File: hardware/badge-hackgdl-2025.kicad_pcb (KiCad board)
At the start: 11 copper layers, 73.4 x 79.5 mm, 57 parts, among them J1 ADDON, J2 Battery, P1 USB_C_Plug_USB2.0, Q1 DMG3415U-7, Q2 MMBT2222A, SW1 ON, SW2 RESET, SW3 BOOT, SW4 RIGHT, SW5 BACK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

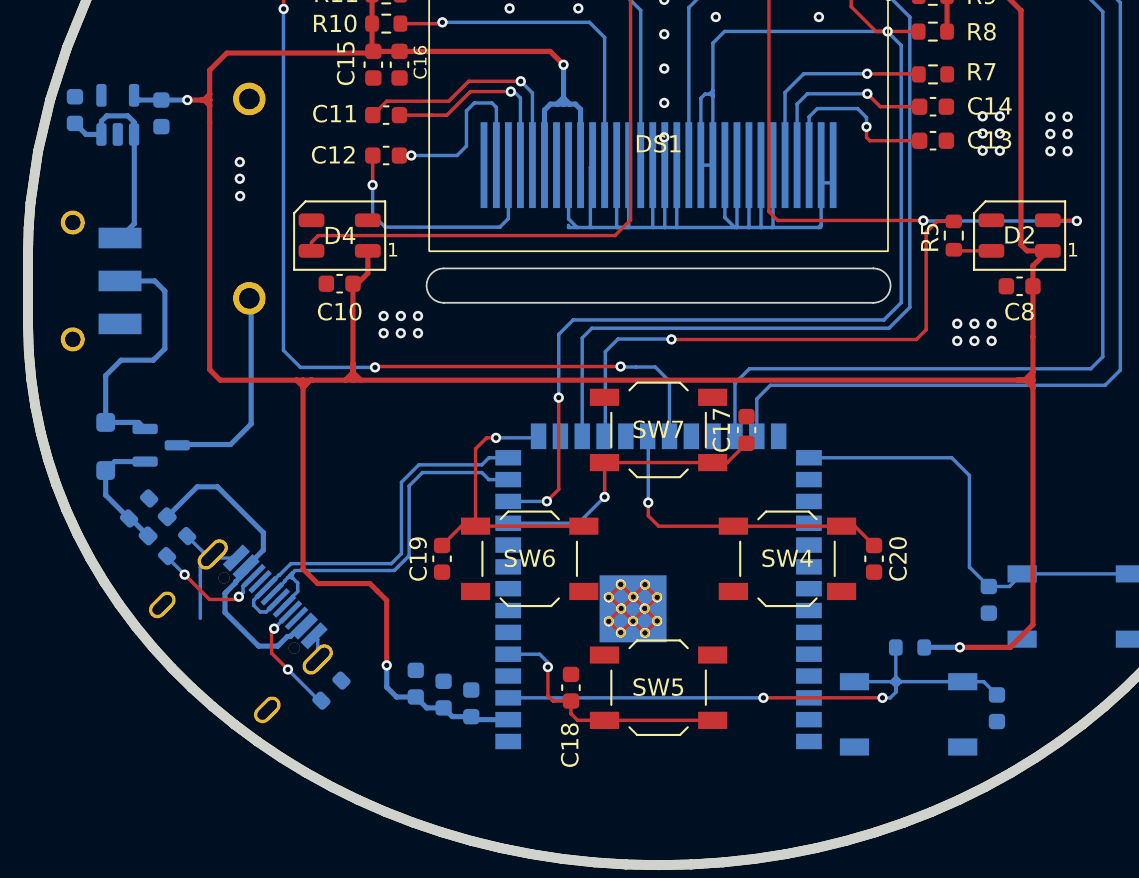
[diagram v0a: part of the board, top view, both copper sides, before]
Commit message: feat(hw): add space between buttons
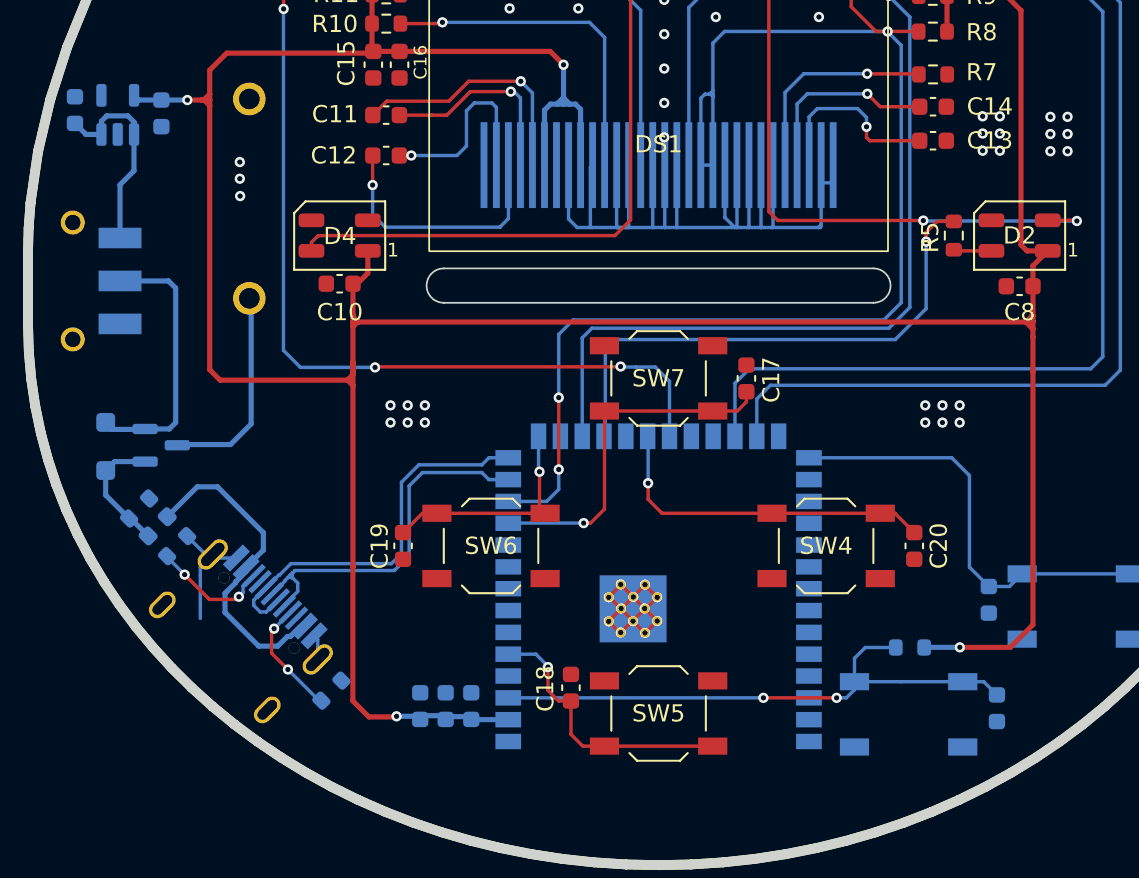
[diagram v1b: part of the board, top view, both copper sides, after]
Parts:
- moved C17 3.00 mm to (138.8, 70.0)
- moved SW7 3.00 mm to (133.7, 70.0)
- moved C20 2.46 mm to (148.6, 79.8)
- moved C19 2.39 mm to (118.8, 79.8)
- moved SW4 2.37 mm to (143.4, 79.8)
- moved SW6 2.37 mm to (123.9, 79.8)
- moved SW5 1.50 mm to (133.7, 89.5)
- moved C3 1.33 mm to (119.8, 89.1)
- moved C4 0.68 mm to (121.3, 89.1)
- moved C5 0.16 mm to (122.8, 89.1)
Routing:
- net /MIDDLE: track 17.0 -> 20.7 mm
- net /LEFT: track 17.2 -> 13.5 mm
- net +3V3: track 250.7 -> 247.8 mm
- net /RST: track 36.2 -> 33.4 mm
- net /RIGHT: track 18.5 -> 20.0 mm
- net /BACK: track 15.1 -> 16.1 mm
- net /NEOPIXEL: track 31.7 -> 31.0 mm
- net GND: track 99.6 -> 98.9 mm

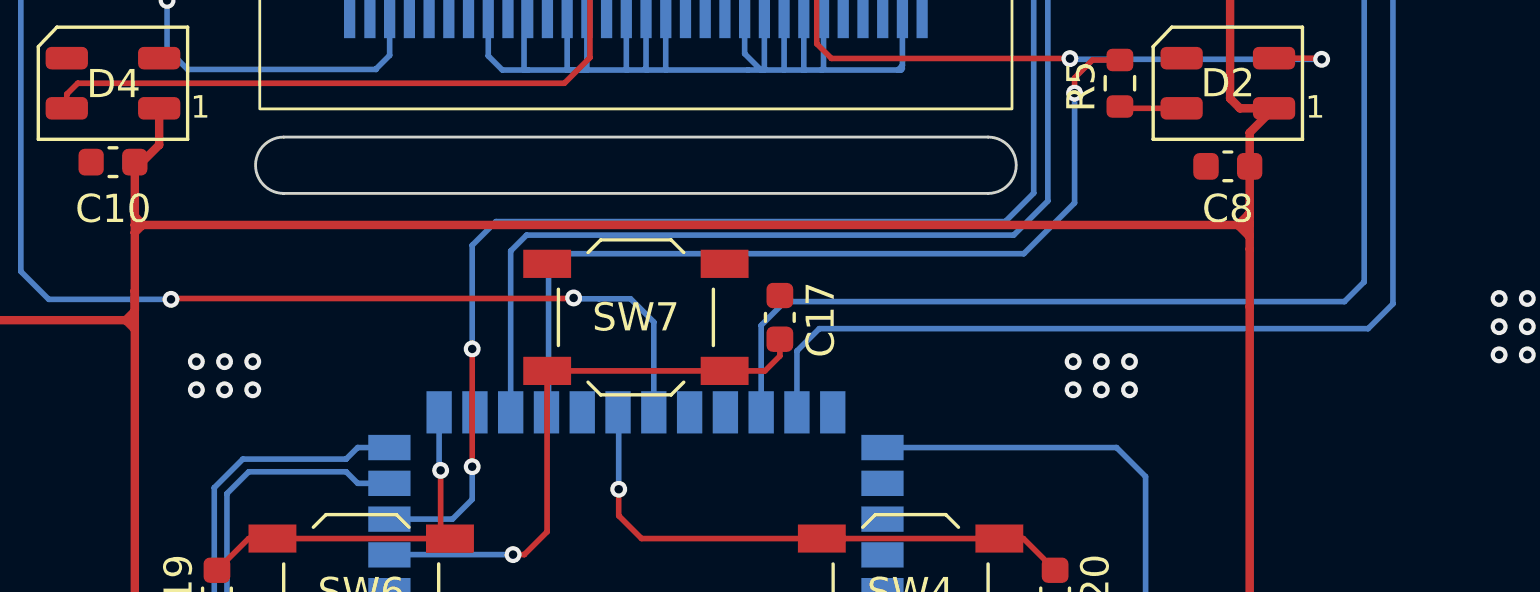
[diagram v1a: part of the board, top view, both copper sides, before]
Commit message: fix(hw): change gpio pins for addon connector
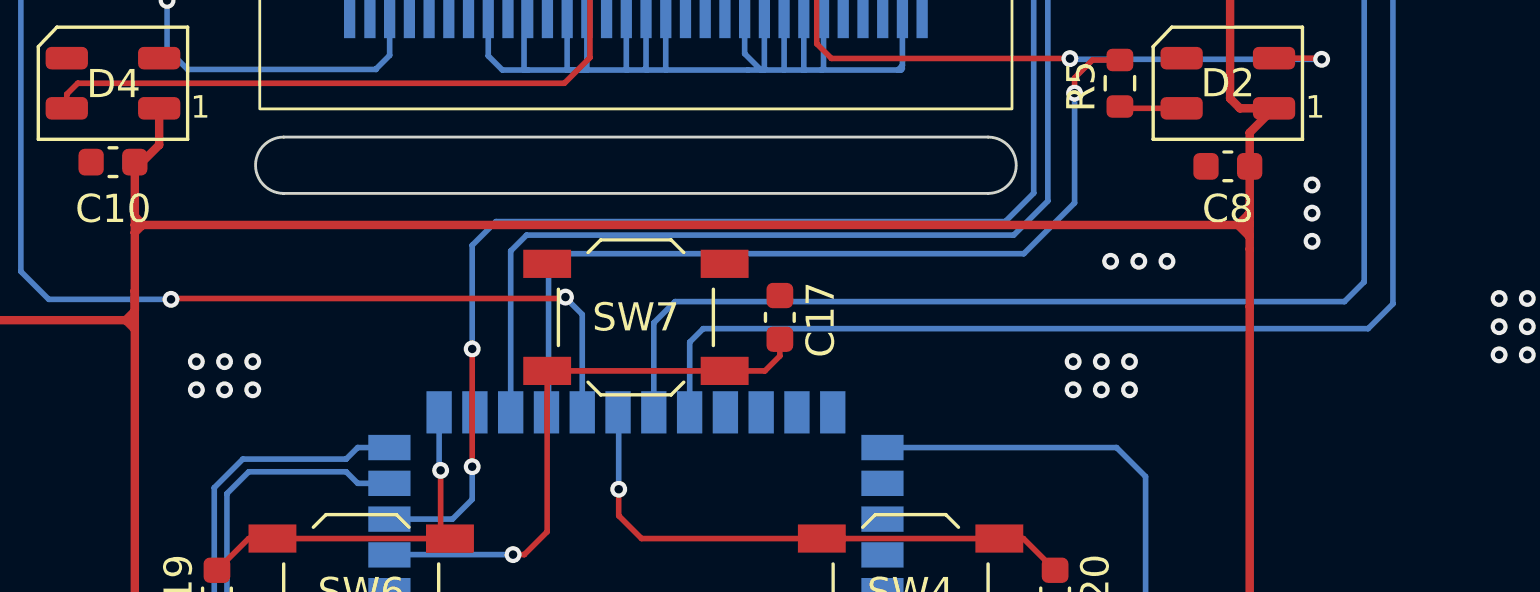
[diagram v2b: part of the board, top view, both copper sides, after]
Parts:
- removed kibuzzard-67869934: G***, kibuzzard-67869934
- removed kibuzzard-67869944: G***, kibuzzard-67869944
- removed kibuzzard-678699AD: G***, kibuzzard-678699AD
- removed kibuzzard-678699B2: G***, kibuzzard-678699B2
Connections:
- U2 pad 19: unconnected-(U2-IO11-Pad19) -> /Buzz
- U2 pad 21: /Buzz -> /GPIO2
- U2 pad 22: unconnected-(U2-IO14-Pad22) -> /GPIO1
- U2 pad 24: /GPIO2 -> unconnected-(U2-IO47-Pad24)
- U2 pad 25: /GPIO1 -> unconnected-(U2-IO48-Pad25)
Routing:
- net /GPIO1: track 73.0 -> 77.0 mm
- net /GPIO2: track 67.6 -> 71.5 mm
- net /Buzz: track 49.6 -> 47.3 mm
- net GND: vias 93 -> 99

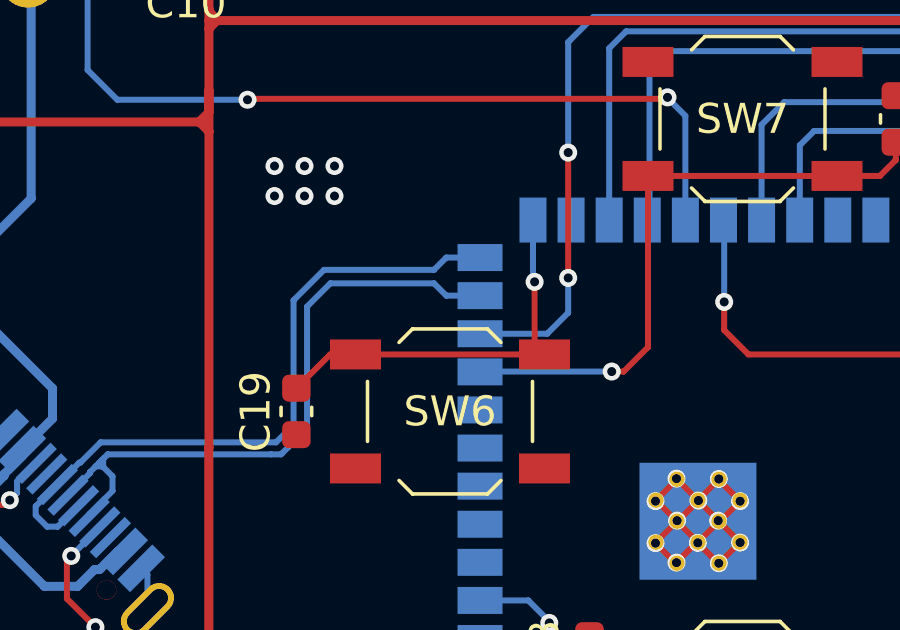
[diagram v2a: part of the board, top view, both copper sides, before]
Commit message: fix(hw): change left button to gpio 17
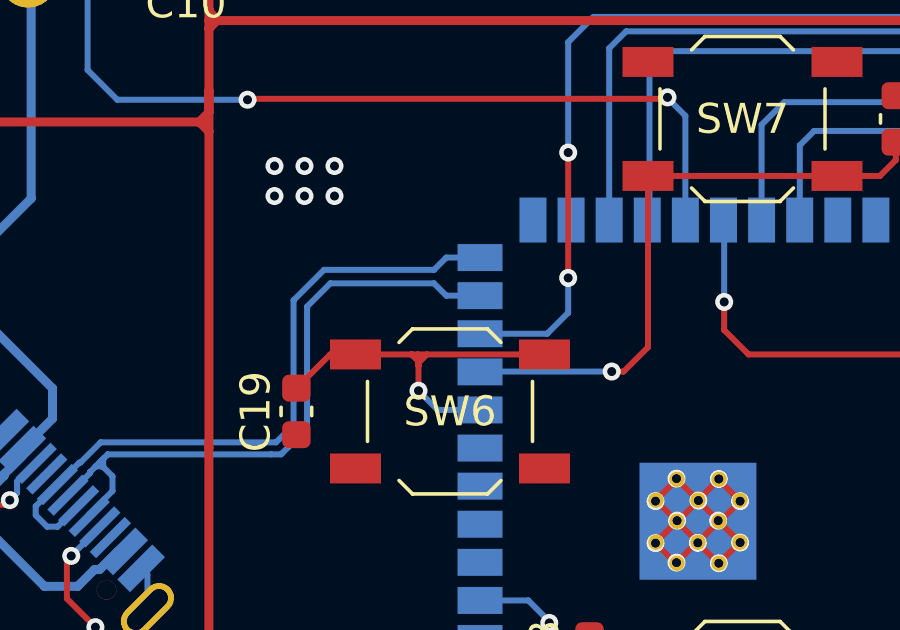
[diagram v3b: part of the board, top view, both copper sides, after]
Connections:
- U2 pad 10: unconnected-(U2-IO17-Pad10) -> /LEFT
- U2 pad 15: /LEFT -> unconnected-(U2-IO3-Pad15)
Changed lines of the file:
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@@
 	(net 59 "unconnected-(U2-IO39-Pad32)")
 	(net 60 "unconnected-(U2-IO36-Pad29)")
-	(net 61 "unconnected-(U2-IO17-Pad10)")
+	(net 61 "unconnected-(U2-IO3-Pad15)")
 	(net 62 "unconnected-(U2-IO15-Pad8)")
 	(net 63 "unconnected-(U2-IO47-Pad24)")
@@
 			(size 1.5 0.9)
 			(layers "B.Cu" "B.Mask" "B.Paste")
-			(net 61 "unconnected-(U2-IO17-Pad10)")
+			(net 16 "/LEFT")
 			(pinfunction "IO17")
-			(pintype "bidirectional+no_connect")
+			(pintype "bidirectional")
 		)
 		(pad "11" smd rect
@@
 			(size 1.5 0.9)
 			(layers "B.Cu" "B.Mask" "B.Paste")
-			(net 16 "/LEFT")
+			(net 61 "unconnected-(U2-IO3-Pad15)")
 			(pinfunction "IO3")
-			(pintype "bidirectional")
+			(pintype "bidirectional+no_connect")
 		)
 		(pad "16" smd rect
@@
 	)
 	(segment
+		(start 122.85 77.88)
+		(end 123.15 77.88)
+		(width 0.2)
+		(layer "F.Cu")
+		(net 16)
+	)
+	(segment
+		(start 122.87 78.25)
+		(end 122.87 78.16)
+		(width 0.2)
+		(layer "F.Cu")
+		(net 16)
+	)
+	(segment
+		(start 122.87 78.16)
+		(end 123.15 77.88)
+		(width 0.2)
+		(layer "F.Cu")
+		(net 16)
+	)
+	(segment
+		(start 122.87 78.16)
+		(end 122.87 78.11)
+		(width 0.2)
+		(layer "F.Cu")
+		(net 16)
+	)
+	(segment
+		(start 122.64 77.88)
+		(end 122.85 77.88)
+		(width 0.2)
+		(layer "F.Cu")
+		(net 16)
+	)
+	(segment
 		(start 120.87 77.88)
 		(end 120.89 77.9)
@@
 	)
 	(segment
-		(start 126.74 77.5499)
-		(end 127.0701 77.88)
+		(start 122.87 77.9)
+		(end 122.85 77.88)
+		(width 0.2)
+		(layer "F.Cu")
+		(net 16)
+	)
+	(segment
+		(start 122.87 78.11)
+		(end 122.64 77.88)
+		(width 0.2)
+		(layer "F.Cu")
+		(net 16)
+	)
+	(segment
+		(start 122.87 79.09)
+		(end 122.87 78.25)
 		(width 0.2)
 		(layer "F.Cu")
@@
 	)
 	(segment
-		(start 120.7701 77.88)
+		(start 123.15 77.88)
 		(end 127.0701 77.88)
 		(width 0.2)
@@
 	)
 	(segment
-		(start 126.74 75.46)
-		(end 126.74 77.5499)
+		(start 120.7701 77.88)
+		(end 122.64 77.88)
+		(width 0.2)
+		(layer "F.Cu")
+		(net 16)
+	)
+	(segment
+		(start 122.87 78.25)
+		(end 122.87 77.9)
 		(width 0.2)
 		(layer "F.Cu")
@@
 	)
 	(via
-		(at 126.74 75.46)
+		(at 122.87 79.09)
 		(size 0.6)
 		(drill 0.3)
@@
 	)
 	(segment
-		(start 126.686189 75.406189)
-		(end 126.686189 73.4)
+		(start 124.921189 79.73)
+		(end 123.51 79.73)
 		(width 0.2)
 		(layer "B.Cu")
@@
 	)
 	(segment
-		(start 126.74 75.46)
-		(end 126.686189 75.406189)
+		(start 123.51 79.73)
+		(end 122.87 79.09)
 		(width 0.2)
 		(layer "B.Cu")

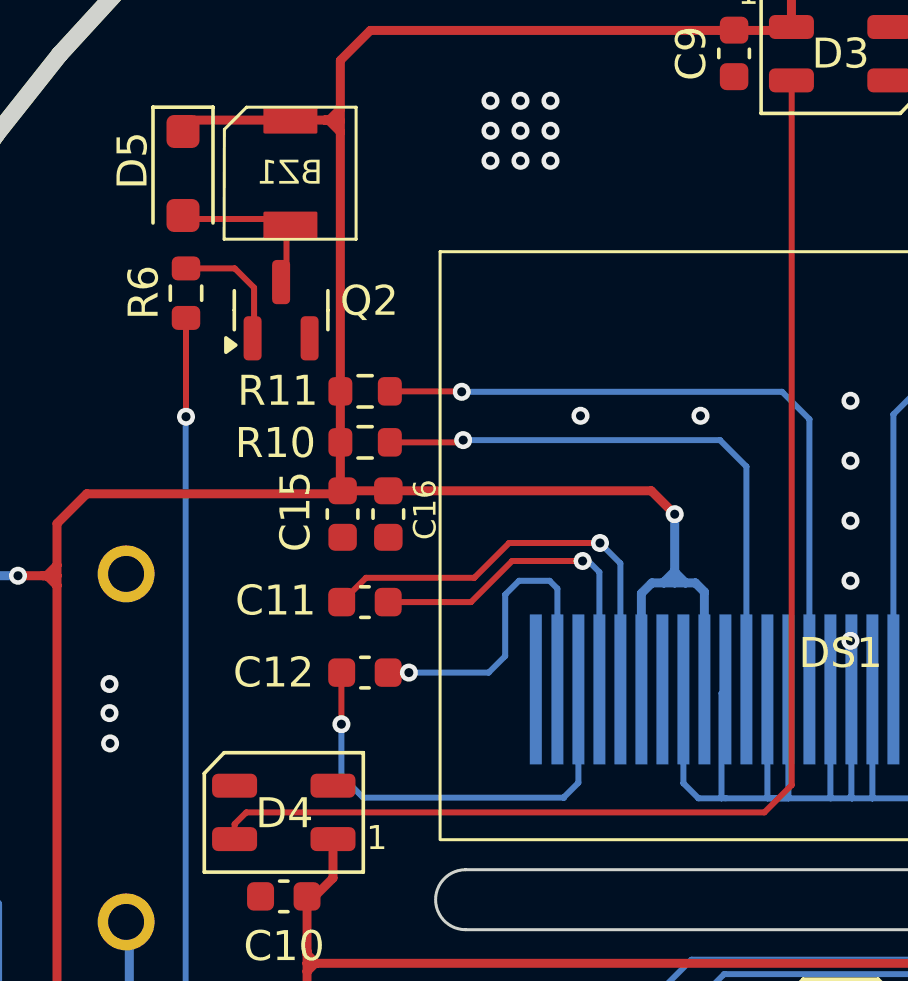
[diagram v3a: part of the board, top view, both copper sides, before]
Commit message: feat(hw): add capacitor in reset pin
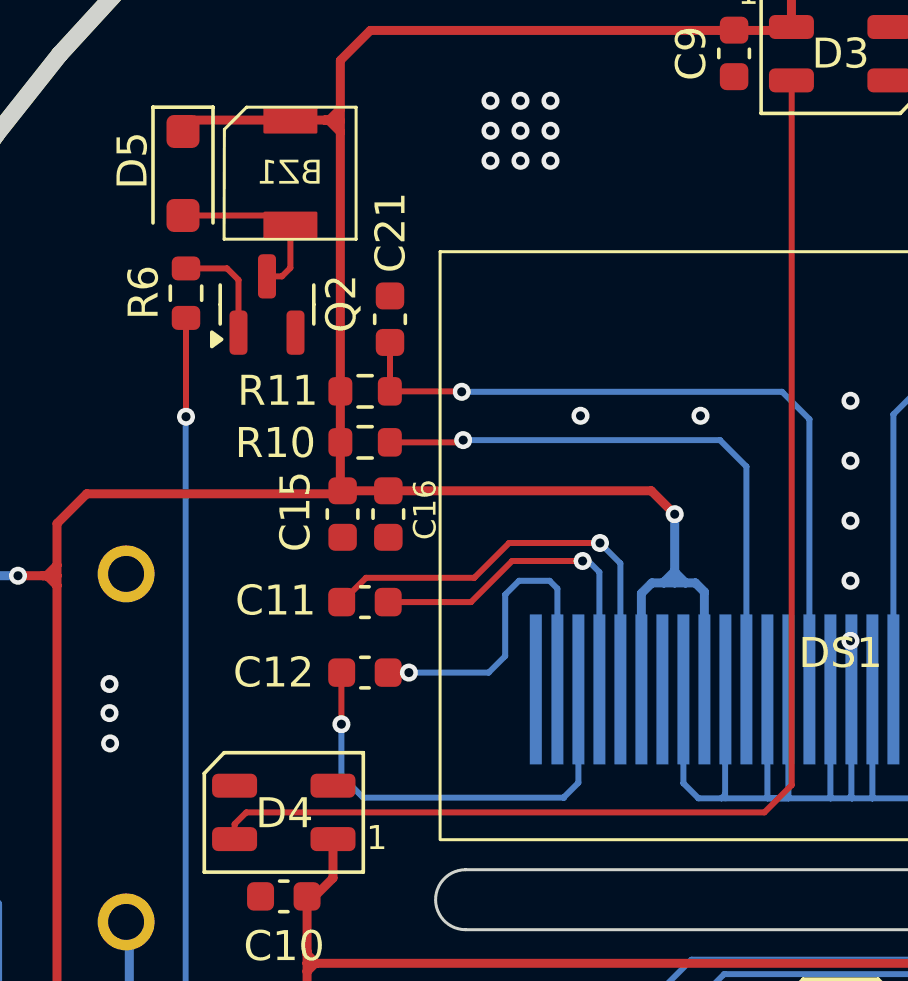
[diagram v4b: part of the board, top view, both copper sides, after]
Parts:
- added C21: 4.7uF, Capacitor_SMD:C_0603_1608Metric, F.Cu at (118.7, 45.3)
- moved Q2 0.51 mm to (114.5, 44.8)
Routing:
- net Net-(DS1-~{RES}): track 23.4 -> 25.0 mm
- net Net-(Q2-B): track 4.24 -> 3.67 mm
